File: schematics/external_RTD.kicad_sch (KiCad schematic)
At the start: 8 parts, among them P1 6-pin header, U1 MAX31865xAP, U3 MAX31865xAP, U4 MAX485E

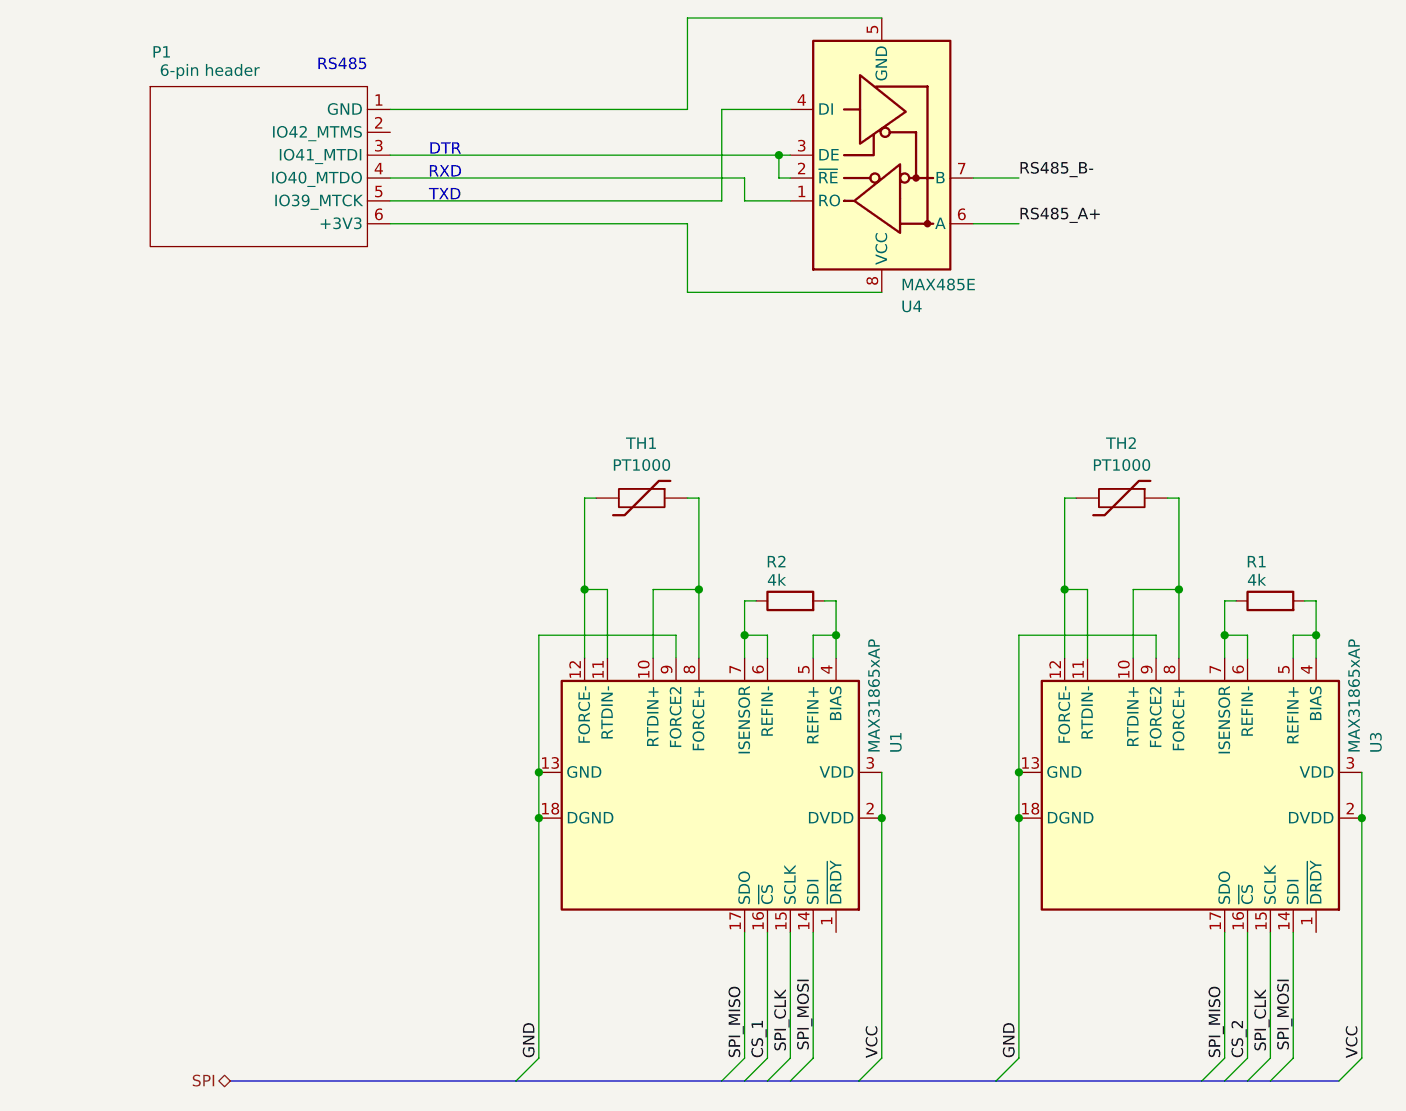
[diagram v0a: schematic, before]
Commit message: chore: more deatils on hierachical schematic
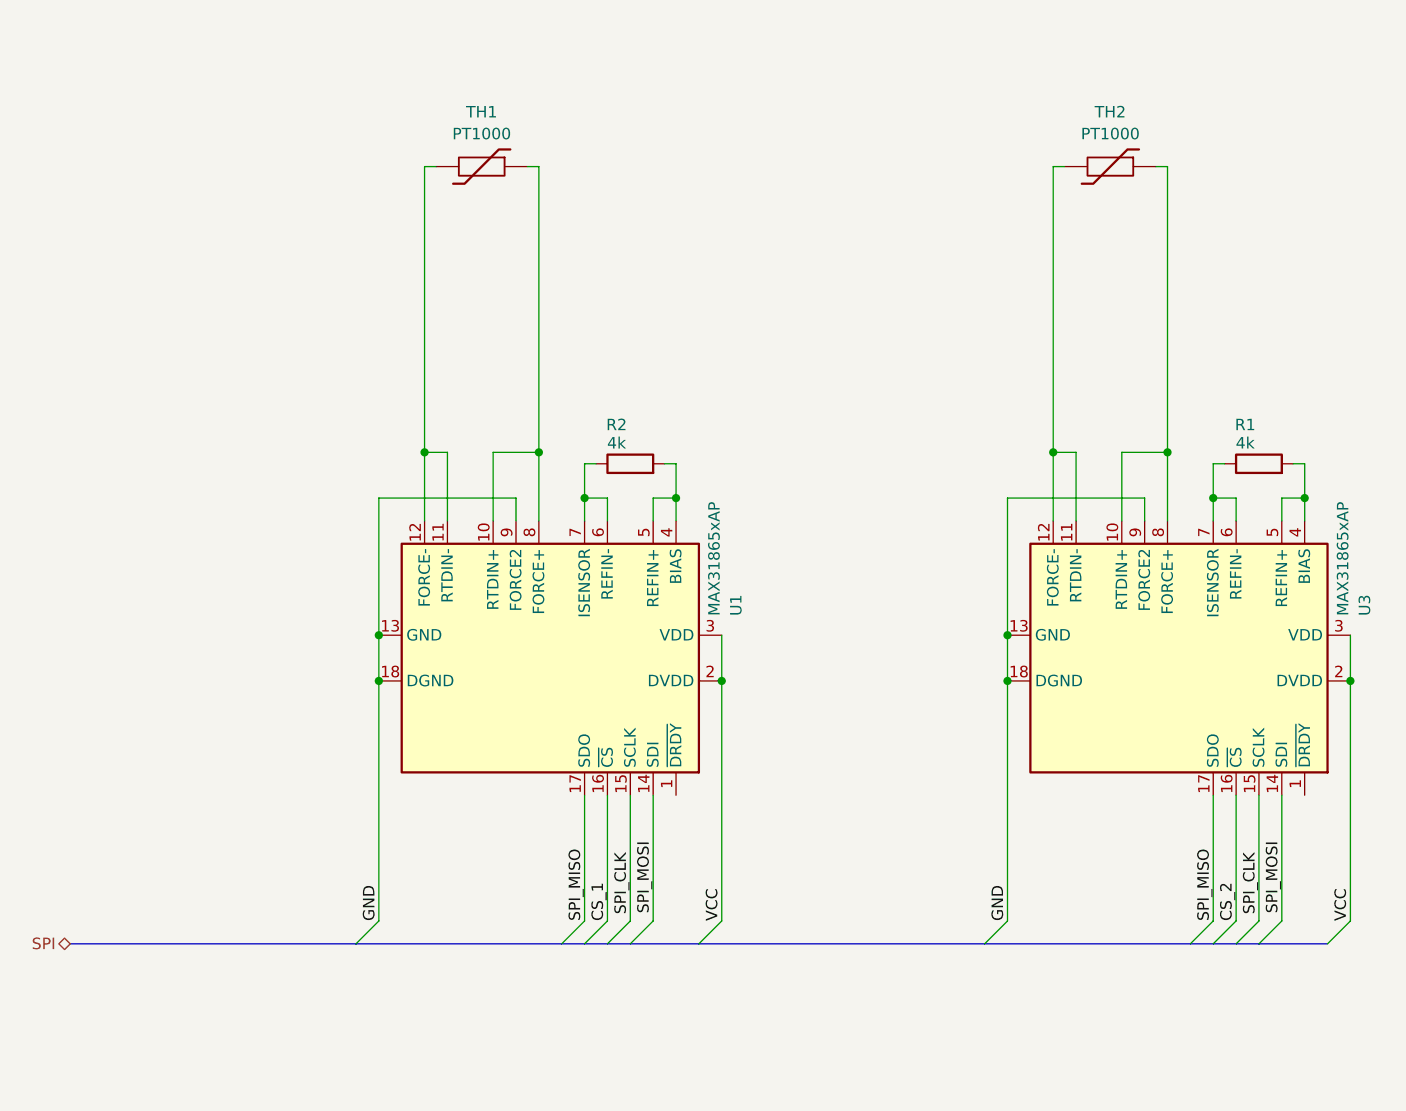
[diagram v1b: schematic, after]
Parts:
- removed P1: 6-pin header, symbol T-Relay6:TRelay6-JtagIO
- removed U4: MAX485E, Package_SO:SOIC-8_3.9x4.9mm_P1.27mm, symbol Interface_UART:MAX485E
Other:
- note removed: "DTR"
- note removed: "RS485"
- note removed: "RXD"
- note removed: "TXD"
- moved on the sheet: R1, R2, TH1, TH2, U1, U3
